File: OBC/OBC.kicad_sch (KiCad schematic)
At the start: 10 parts, among them J2 IDC1 (PMS-Raspi), J3 IDC2 (Raspi-TRU), J5 Conn_01x04, J6 Modo de operación, U1 MPU9250, U2 BMP280, U3 RASPBERRY_PI_ZERO_2_W

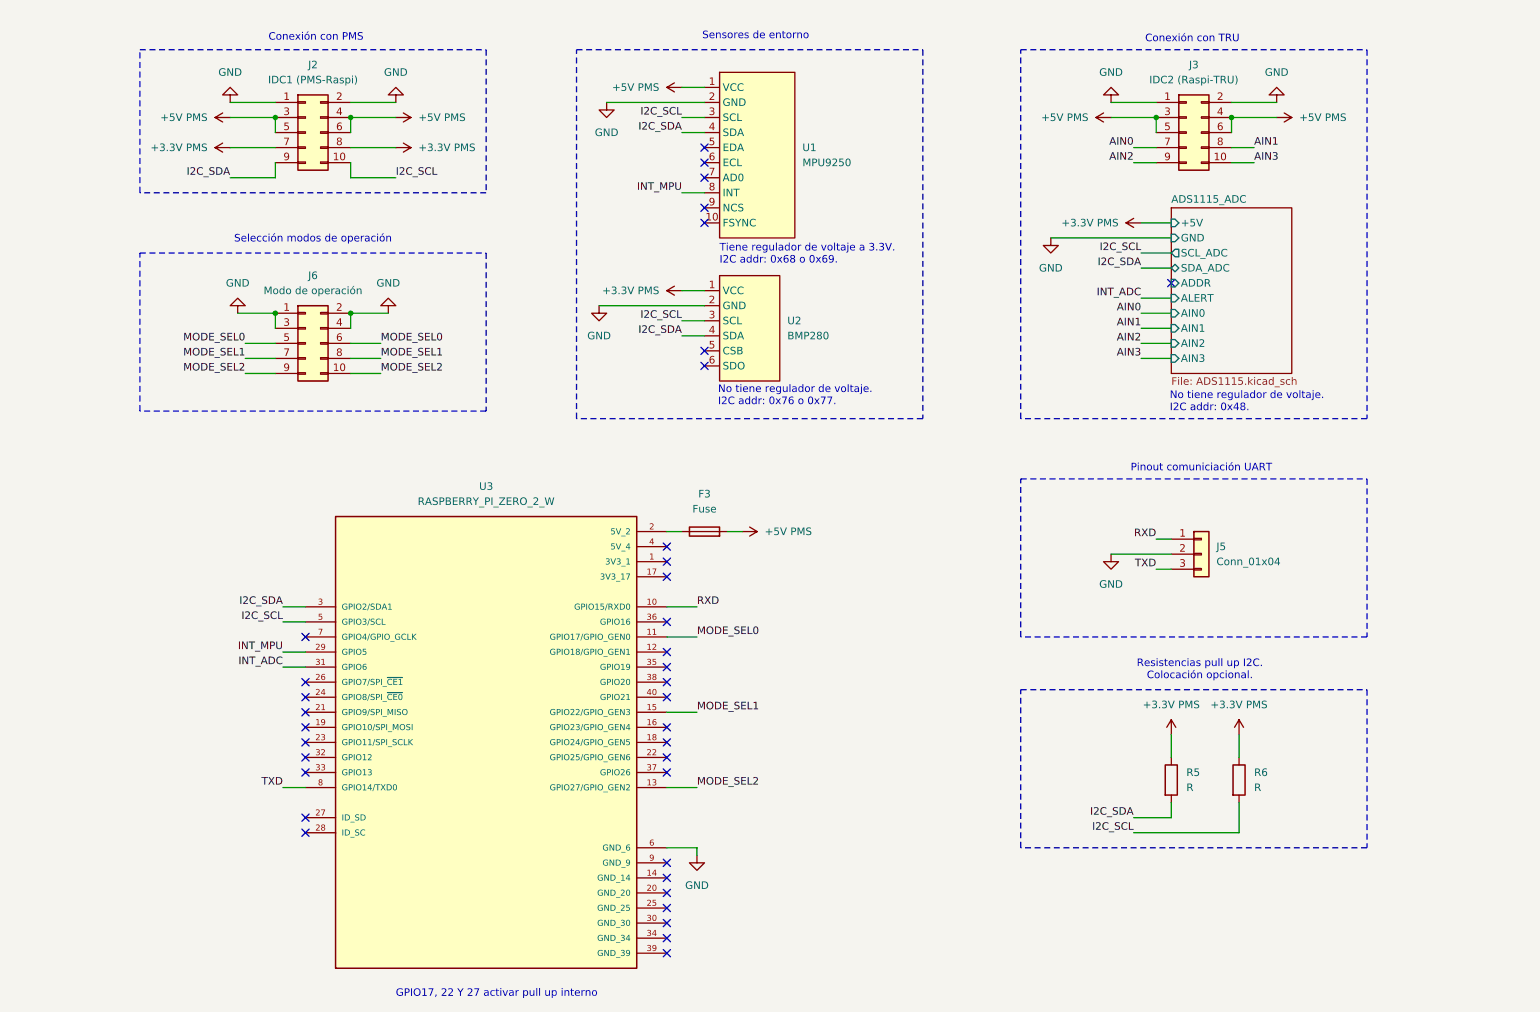
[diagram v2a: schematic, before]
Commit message: Actualiza numeración de componentes
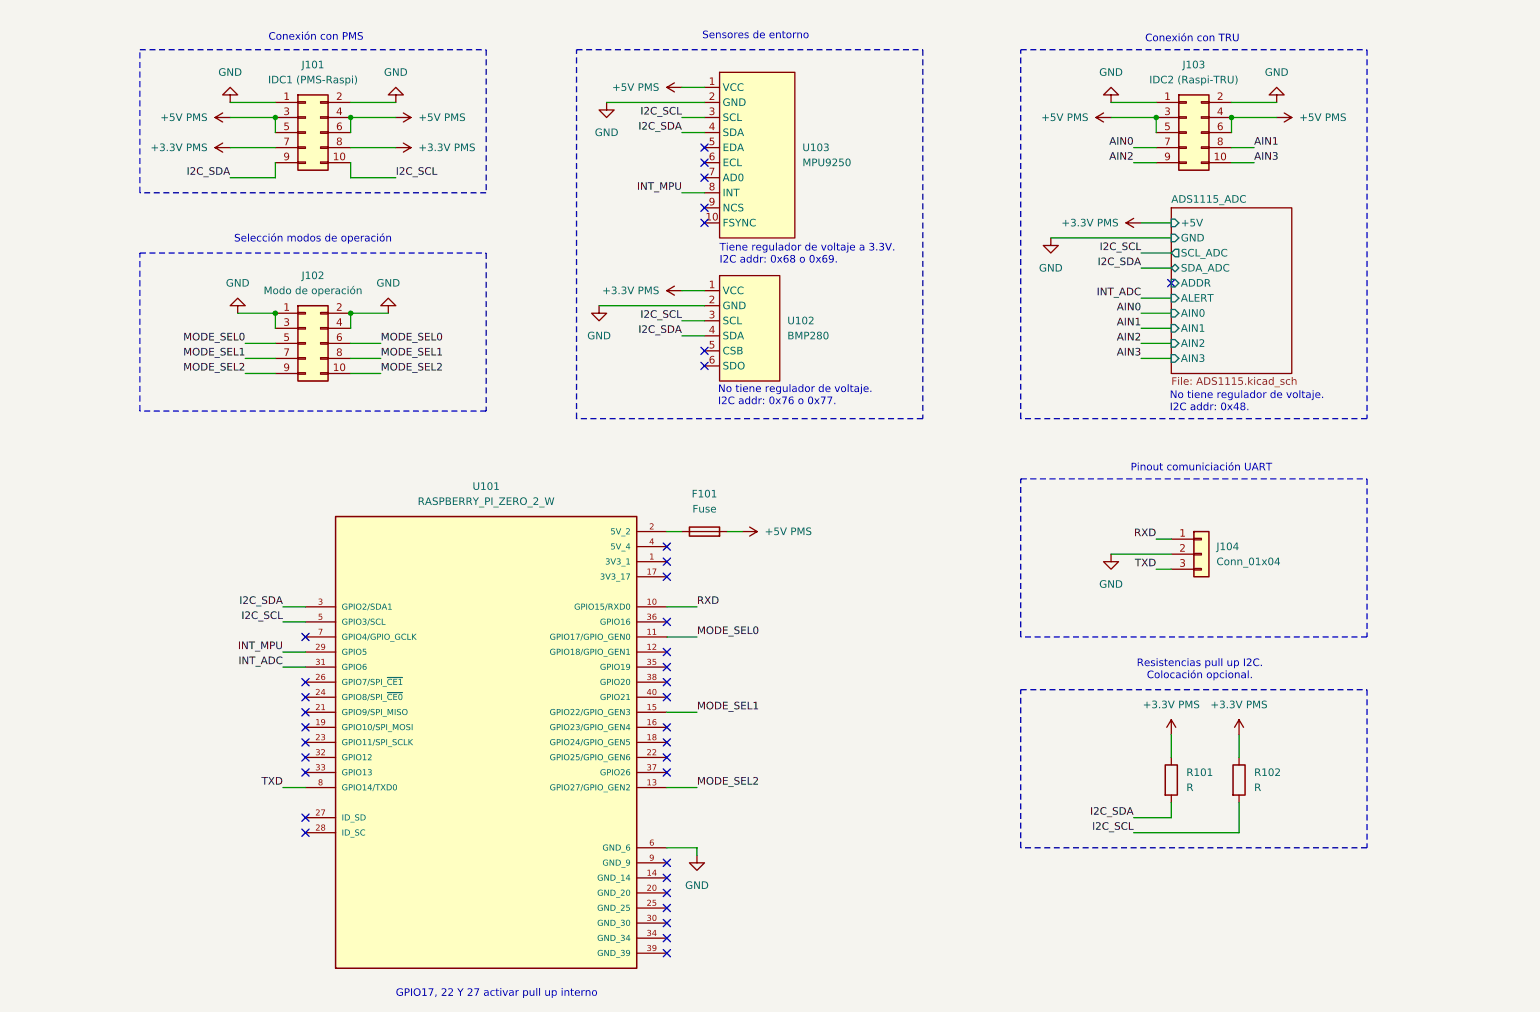
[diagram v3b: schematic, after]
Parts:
- renumbered F3 to F101, J2 to J101, J6 to J102, J3 to J103, J5 to J104, R5 to R101, R6 to R102, U3 to U101, U2 to U102, U1 to U103
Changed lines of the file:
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@@
 		(dnp no)
 		(fields_autoplaced yes)
-		(property "Reference" "#PWR07"
+		(property "Reference" "#PWR0119"
 			(at 214.63 55.88 0)
 			(effects
@@
 			(project "OBC"
 				(path "/1029d1d3-4fe2-46fb-aa7d-396827b97897"
-					(reference "#PWR07")
+					(reference "#PWR0119")
 					(unit 1)
 				)
@@
 		(dnp no)
 		(fields_autoplaced yes)
-		(property "Reference" "#PWR014"
+		(property "Reference" "#PWR0116"
 			(at 205.74 29.21 0)
 			(effects
@@
 			(project "OBC"
 				(path "/1029d1d3-4fe2-46fb-aa7d-396827b97897"
-					(reference "#PWR014")
+					(reference "#PWR0116")
 					(unit 1)
 				)
@@
 		(dnp no)
 		(fields_autoplaced yes)
-		(property "Reference" "#PWR02"
+		(property "Reference" "#PWR0107"
 			(at 81.28 38.1 0)
 			(effects
@@
 			(project ""
 				(path "/1029d1d3-4fe2-46fb-aa7d-396827b97897"
-					(reference "#PWR02")
+					(reference "#PWR0107")
 					(unit 1)
 				)
@@
 		(dnp no)
 		(fields_autoplaced yes)
-		(property "Reference" "#PWR020"
+		(property "Reference" "#PWR0104"
 			(at 58.42 64.77 0)
 			(effects
@@
 			(project "OBC"
 				(path "/1029d1d3-4fe2-46fb-aa7d-396827b97897"
-					(reference "#PWR020")
+					(reference "#PWR0104")
 					(unit 1)
 				)
@@
 		(dnp no)
 		(fields_autoplaced yes)
-		(property "Reference" "#PWR017"
+		(property "Reference" "#PWR0120"
 			(at 215.9 146.05 0)
 			(effects
@@
 			(project "OBC"
 				(path "/1029d1d3-4fe2-46fb-aa7d-396827b97897"
-					(reference "#PWR017")
+					(reference "#PWR0120")
 					(unit 1)
 				)
@@
 		(dnp no)
 		(fields_autoplaced yes)
-		(property "Reference" "#PWR011"
+		(property "Reference" "#PWR0109"
 			(at 119.38 76.2 0)
 			(effects
@@
 			(project "OBC"
 				(path "/1029d1d3-4fe2-46fb-aa7d-396827b97897"
-					(reference "#PWR011")
+					(reference "#PWR0109")
 					(unit 1)
 				)
@@
 		(dnp no)
 		(fields_autoplaced yes)
-		(property "Reference" "#PWR04"
+		(property "Reference" "#PWR0102"
 			(at 60.96 38.1 0)
 			(effects
@@
 			(project "OBC"
 				(path "/1029d1d3-4fe2-46fb-aa7d-396827b97897"
-					(reference "#PWR04")
+					(reference "#PWR0102")
 					(unit 1)
 				)
@@
 		(dnp no)
 		(fields_autoplaced yes)
-		(property "Reference" "#PWR01"
+		(property "Reference" "#PWR0101"
 			(at 57.15 29.21 0)
 			(effects
@@
 			(project ""
 				(path "/1029d1d3-4fe2-46fb-aa7d-396827b97897"
-					(reference "#PWR01")
+					(reference "#PWR0101")
 					(unit 1)
 				)
@@
 		(dnp no)
 		(fields_autoplaced yes)
-		(property "Reference" "R6"
+		(property "Reference" "R102"
 			(at 229.87 148.5899 0)
 			(effects
@@
 			(project "OBC"
 				(path "/1029d1d3-4fe2-46fb-aa7d-396827b97897"
-					(reference "R6")
+					(reference "R102")
 					(unit 1)
 				)
@@
 		(dnp no)
 		(fields_autoplaced yes)
-		(property "Reference" "#PWR09"
+		(property "Reference" "#PWR0105"
 			(at 83.82 64.77 0)
 			(effects
@@
 			(project "OBC"
 				(path "/1029d1d3-4fe2-46fb-aa7d-396827b97897"
-					(reference "#PWR09")
+					(reference "#PWR0105")
 					(unit 1)
 				)
@@
 		(dnp no)
 		(fields_autoplaced yes)
-		(property "Reference" "#PWR08"
+		(property "Reference" "#PWR0115"
 			(at 195.58 64.77 0)
 			(effects
@@
 			(project "OBC"
 				(path "/1029d1d3-4fe2-46fb-aa7d-396827b97897"
-					(reference "#PWR08")
+					(reference "#PWR0115")
 					(unit 1)
 				)
@@
 		(dnp no)
 		(fields_autoplaced yes)
-		(property "Reference" "U2"
+		(property "Reference" "U102"
 			(at 151.13 72.3899 0)
 			(effects
@@
 			(project ""
 				(path "/1029d1d3-4fe2-46fb-aa7d-396827b97897"
-					(reference "U2")
+					(reference "U102")
 					(unit 1)
 				)
@@
 		(dnp no)
 		(fields_autoplaced yes)
-		(property "Reference" "#PWR010"
+		(property "Reference" "#PWR0110"
 			(at 120.65 41.91 0)
 			(effects
@@
 			(project "OBC"
 				(path "/1029d1d3-4fe2-46fb-aa7d-396827b97897"
-					(reference "#PWR010")
+					(reference "#PWR0110")
 					(unit 1)
 				)
@@
 		(dnp no)
 		(fields_autoplaced yes)
-		(property "Reference" "#PWR018"
+		(property "Reference" "#PWR0121"
 			(at 227.33 146.05 0)
 			(effects
@@
 			(project "OBC"
 				(path "/1029d1d3-4fe2-46fb-aa7d-396827b97897"
-					(reference "#PWR018")
+					(reference "#PWR0121")
 					(unit 1)
 				)
@@
 		(dnp no)
 		(fields_autoplaced yes)
-		(property "Reference" "#PWR024"
+		(property "Reference" "#PWR0123"
 			(at 229.87 38.1 0)
 			(effects
@@
 			(project "OBC"
 				(path "/1029d1d3-4fe2-46fb-aa7d-396827b97897"
-					(reference "#PWR024")
+					(reference "#PWR0123")
 					(unit 1)
 				)
@@
 		(on_board yes)
 		(dnp no)
-		(property "Reference" "U1"
+		(property "Reference" "U103"
 			(at 153.67 43.1799 0)
 			(effects
@@
 			(project ""
 				(path "/1029d1d3-4fe2-46fb-aa7d-396827b97897"
-					(reference "U1")
+					(reference "U103")
 					(unit 1)
 				)
@@
 		(dnp no)
 		(fields_autoplaced yes)
-		(property "Reference" "#PWR019"
+		(property "Reference" "#PWR0111"
 			(at 137.16 33.02 0)
 			(effects
@@
 			(project "OBC"
 				(path "/1029d1d3-4fe2-46fb-aa7d-396827b97897"
-					(reference "#PWR019")
+					(reference "#PWR0111")
 					(unit 1)
 				)
@@
 		(dnp no)
 		(fields_autoplaced yes)
-		(property "Reference" "J3"
+		(property "Reference" "J103"
 			(at 219.71 29.21 0)
 			(effects
@@
 			(project "OBC"
 				(path "/1029d1d3-4fe2-46fb-aa7d-396827b97897"
-					(reference "J3")
+					(reference "J103")
 					(unit 1)
 				)
@@
 		(dnp no)
 		(fields_autoplaced yes)
-		(property "Reference" "#PWR06"
+		(property "Reference" "#PWR0106"
 			(at 85.09 29.21 0)
 			(effects
@@
 			(project "OBC"
 				(path "/1029d1d3-4fe2-46fb-aa7d-396827b97897"
-					(reference "#PWR06")
+					(reference "#PWR0106")
 					(unit 1)
 				)
@@
 		(dnp no)
 		(fields_autoplaced yes)
-		(property "Reference" "#PWR05"
+		(property "Reference" "#PWR0103"
 			(at 60.96 43.18 0)
 			(effects
@@
 			(project "OBC"
 				(path "/1029d1d3-4fe2-46fb-aa7d-396827b97897"
-					(reference "#PWR05")
+					(reference "#PWR0103")
 					(unit 1)
 				)
@@
 		(dnp no)
 		(fields_autoplaced yes)
-		(property "Reference" "#PWR012"
+		(property "Reference" "#PWR0112"
 			(at 137.16 67.31 0)
 			(effects
@@
 			(project "OBC"
 				(path "/1029d1d3-4fe2-46fb-aa7d-396827b97897"
-					(reference "#PWR012")
+					(reference "#PWR0112")
 					(unit 1)
 				)
@@
 		(dnp no)
 		(fields_autoplaced yes)
-		(property "Reference" "#PWR015"
+		(property "Reference" "#PWR0113"
 			(at 135.89 168.91 0)
 			(effects
@@
 			(project "OBC"
 				(path "/1029d1d3-4fe2-46fb-aa7d-396827b97897"
-					(reference "#PWR015")
+					(reference "#PWR0113")
 					(unit 1)
 				)
@@
 		(dnp no)
 		(fields_autoplaced yes)
-		(property "Reference" "#PWR013"
+		(property "Reference" "#PWR0122"
 			(at 233.68 29.21 0)
 			(effects
@@
 			(project "OBC"
 				(path "/1029d1d3-4fe2-46fb-aa7d-396827b97897"
-					(reference "#PWR013")
+					(reference "#PWR0122")
 					(unit 1)
 				)
@@
 		(dnp no)
 		(fields_autoplaced yes)
-		(property "Reference" "J6"
+		(property "Reference" "J102"
 			(at 71.12 64.77 0)
 			(effects
@@
 			(project "OBC"
 				(path "/1029d1d3-4fe2-46fb-aa7d-396827b97897"
-					(reference "J6")
+					(reference "J102")
 					(unit 1)
 				)
@@
 		(dnp no)
 		(fields_autoplaced yes)
-		(property "Reference" "F3"
+		(property "Reference" "F101"
 			(at 137.16 101.6 90)
 			(effects
@@
 			(project ""
 				(path "/1029d1d3-4fe2-46fb-aa7d-396827b97897"
-					(reference "F3")
+					(reference "F101")
 					(unit 1)
 				)
@@
 		(dnp no)
 		(fields_autoplaced yes)
-		(property "Reference" "#PWR03"
+		(property "Reference" "#PWR0108"
 			(at 81.28 43.18 0)
 			(effects
@@
 			(project ""
 				(path "/1029d1d3-4fe2-46fb-aa7d-396827b97897"
-					(reference "#PWR03")
+					(reference "#PWR0108")
 					(unit 1)
 				)
@@
 		(dnp no)
 		(fields_autoplaced yes)
-		(property "Reference" "R5"
+		(property "Reference" "R101"
 			(at 218.44 148.5899 0)
 			(effects
@@
 			(project ""
 				(path "/1029d1d3-4fe2-46fb-aa7d-396827b97897"
-					(reference "R5")
+					(reference "R101")
 					(unit 1)
 				)
@@
 		(on_board yes)
 		(dnp no)
-		(property "Reference" "#PWR025"
+		(property "Reference" "#PWR0117"
 			(at 209.55 38.1 0)
 			(effects
@@
 			(project "OBC"
 				(path "/1029d1d3-4fe2-46fb-aa7d-396827b97897"
-					(reference "#PWR025")
+					(reference "#PWR0117")
 					(unit 1)
 				)
@@
 		(dnp no)
 		(fields_autoplaced yes)
-		(property "Reference" "#PWR016"
+		(property "Reference" "#PWR0114"
 			(at 139.7 107.95 0)
 			(effects
@@
 			(project "OBC"
 				(path "/1029d1d3-4fe2-46fb-aa7d-396827b97897"
-					(reference "#PWR016")
+					(reference "#PWR0114")
 					(unit 1)
 				)
@@
 		(dnp no)
 		(fields_autoplaced yes)
-		(property "Reference" "J2"
+		(property "Reference" "J101"
 			(at 71.12 29.21 0)
 			(effects
@@
 			(project ""
 				(path "/1029d1d3-4fe2-46fb-aa7d-396827b97897"
-					(reference "J2")
+					(reference "J101")
 					(unit 1)
 				)
@@
 		(dnp no)
 		(fields_autoplaced yes)
-		(property "Reference" "J5"
+		(property "Reference" "J104"
 			(at 223.52 110.4899 0)
 			(effects
@@
 			(project ""
 				(path "/1029d1d3-4fe2-46fb-aa7d-396827b97897"
-					(reference "J5")
+					(reference "J104")
 					(unit 1)
 				)
@@
 		(dnp no)
 		(fields_autoplaced yes)
-		(property "Reference" "U3"
+		(property "Reference" "U101"
 			(at 100.33 100.33 0)
 			(effects
@@
 			(project ""
 				(path "/1029d1d3-4fe2-46fb-aa7d-396827b97897"
-					(reference "U3")
+					(reference "U101")
 					(unit 1)
 				)
@@
 		(dnp no)
 		(fields_autoplaced yes)
-		(property "Reference" "#PWR021"
+		(property "Reference" "#PWR0118"
 			(at 205.74 118.11 0)
 			(effects
@@
 			(project "OBC"
 				(path "/1029d1d3-4fe2-46fb-aa7d-396827b97897"
-					(reference "#PWR021")
-					(unit 1)
-				)
+					(reference "#PWR0118")
+					(unit 1)
+				)

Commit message: Agrega pwr flags
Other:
- moved on the sheet: F101, J101, J102, J103, J104, R101, R102, U101, U102, U103

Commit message: Agrega footprint rpi
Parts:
- U101: footprint RASPBERRY_PI_ZERO_2_W:MODULE_RASPBERRY_PI_ZERO_2_W -> cubesat:MODULE_RASPBERRY_PI_ZERO_2_W
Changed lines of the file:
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@@
 			)
 		)
-		(property "Footprint" "RASPBERRY_PI_ZERO_2_W:MODULE_RASPBERRY_PI_ZERO_2_W"
+		(property "Footprint" "cubesat:MODULE_RASPBERRY_PI_ZERO_2_W"
 			(at 82.55 142.24 0)
 			(effects
